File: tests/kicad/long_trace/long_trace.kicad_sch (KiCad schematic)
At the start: 2 parts

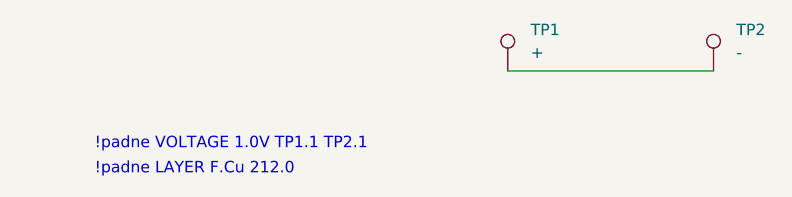
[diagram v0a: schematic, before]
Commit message: feat: Rudimentary stackup spec support
Still veeeeeery TBD
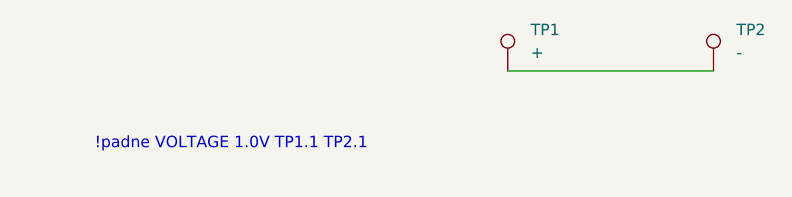
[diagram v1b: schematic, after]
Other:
- note removed: "!padne LAYER F.Cu 212.0"
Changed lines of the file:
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@@
-		)
-	)
-	(text "!padne LAYER F.Cu 212.0"
-		(exclude_from_sim no)
-		(at 75.692 109.982 0)
-		(effects
-			(font
-				(size 1.27 1.27)
-			)
 		)
 	)

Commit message: feat: Richer directive syntax
This commit adds support for named directive parameters. No more
guessing which parameter is the positive terminal positive and which is the
negative terminal!
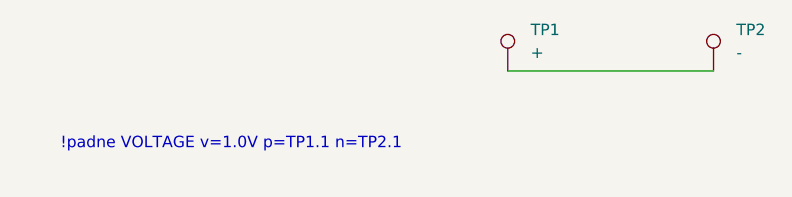
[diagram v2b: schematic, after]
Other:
- note added: "!padne VOLTAGE v=1.0V p=TP1.1 n=TP2.1"
- note removed: "!padne VOLTAGE 1.0V TP1.1 TP2.1"
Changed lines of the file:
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@@
 		)
 	)
-	(text "!padne VOLTAGE 1.0V TP1.1 TP2.1"
+	(text "!padne VOLTAGE v=1.0V p=TP1.1 n=TP2.1"
 		(exclude_from_sim no)
 		(at 79.756 107.188 0)
